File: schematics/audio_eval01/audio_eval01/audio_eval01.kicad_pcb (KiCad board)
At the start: 2 copper layers, 31.1 x 28.6 mm, 2 parts, among them J1 Conn_01x08_Pin

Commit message: Audio evaluation board work.
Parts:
- added C1: 0.1uF, Capacitor_SMD:C_0805_2012Metric_Pad1.18x1.45mm_HandSolder, F.Cu at (136.1, 83.0)
- added C10: 0.1uF, Capacitor_SMD:C_0805_2012Metric_Pad1.18x1.45mm_HandSolder, F.Cu at (150.5, 79.5)
- added C11: 22uF, Capacitor_SMD:C_0805_2012Metric_Pad1.18x1.45mm_HandSolder, F.Cu at (153.0, 79.5)
- added C12: 0.1uF, Capacitor_SMD:C_0805_2012Metric_Pad1.18x1.45mm_HandSolder, F.Cu at (144.8, 76.6)
- added C13: 10uF, Capacitor_SMD:C_0805_2012Metric_Pad1.18x1.45mm_HandSolder, F.Cu at (144.8, 74.0)
- added C2: 10uF, Capacitor_SMD:C_0805_2012Metric_Pad1.18x1.45mm_HandSolder, F.Cu at (138.6, 83.0)
- added C25: 47uF, Capacitor_Tantalum_SMD:CP_EIA-3216-18_Kemet-A, F.Cu at (152.0, 95.4)
- added C3: 10uF, Capacitor_SMD:C_0805_2012Metric_Pad1.18x1.45mm_HandSolder, F.Cu at (138.8, 99.2)
- added C4: 0.1uF, Capacitor_SMD:C_0805_2012Metric_Pad1.18x1.45mm_HandSolder, F.Cu at (137.0, 78.5)
- added C5: 10uF, Capacitor_SMD:C_0805_2012Metric_Pad1.18x1.45mm_HandSolder, F.Cu at (139.5, 78.5)
- added C6: 0.1uF, Capacitor_SMD:C_0805_2012Metric_Pad1.18x1.45mm_HandSolder, F.Cu at (150.5, 88.5)
- added C7: 10uF, Capacitor_SMD:C_0805_2012Metric_Pad1.18x1.45mm_HandSolder, F.Cu at (153.0, 88.5)
- added C8: 0.1uF, Capacitor_SMD:C_0805_2012Metric_Pad1.18x1.45mm_HandSolder, F.Cu at (153.0, 84.0)
- added C9: 22uF, Capacitor_SMD:C_0805_2012Metric_Pad1.18x1.45mm_HandSolder, F.Cu at (150.5, 84.0)
- added J2: AudioJack3, Connector_Audio:Jack_3.5mm_Switronic_ST-005-G_horizontal, F.Cu at (166.9, 94.2)
- added J3: Conn_01x02_Pin, Connector_PinHeader_2.54mm:PinHeader_1x02_P2.54mm_Vertical, F.Cu at (168.8, 78.5)
- added R1: R, Resistor_SMD:R_0805_2012Metric_Pad1.20x1.40mm_HandSolder, F.Cu at (142.0, 89.0)
- added R3: R, Resistor_SMD:R_0805_2012Metric_Pad1.20x1.40mm_HandSolder, F.Cu at (144.5, 89.0)
- added U2: AMS1117-1.8, Package_TO_SOT_SMD:SOT-223-3_TabPin2, F.Cu at (145.6, 96.7)
- J1: value Conn_01x08_Pin -> Conn_01x10_Pin; footprint Connector_PinHeader_2.54mm:PinHeader_1x08_P2.54mm_Vertical -> Connector_PinHeader_2.54mm:PinHeader_1x10_P2.54mm_Vertical
- moved U1 4.91 mm to (145.1, 83.0)
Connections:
- J1 pad 1: WCLK -> GND
- J1 pad 2: BCLK -> GPIO1
- J1 pad 3: MCLK -> DIN
- J1 pad 4: SDA -> WCLK
- J1 pad 5: SCL -> BCLK
- J1 pad 6: unconnected-(J1-Pin_6-Pad6) -> MCLK
- J1 pad 7: unconnected-(J1-Pin_7-Pad7) -> SDA
- J1 pad 8: GPIO1 -> SCL
- U1 pad 13: unconnected-(U1-AIN1-Pad13) -> GND
- U1 pad 14: unconnected-(U1-AIN2-Pad14) -> GND
- U1 pad 17: unconnected-(U1-AVDD-Pad17) -> 3V3
- U1 pad 19: unconnected-(U1-SPKM-Pad19) -> Net-(J3-Pin_1)
- U1 pad 2: unconnected-(U1-IOVDD-Pad2) -> 3V3
- U1 pad 21: unconnected-(U1-SPKVDD-Pad21) -> 5V0
- U1 pad 22: unconnected-(U1-SPKP-Pad22) -> Net-(J3-Pin_2)
- U1 pad 23: unconnected-(U1-SPKM-Pad23) -> Net-(J3-Pin_1)
- U1 pad 24: unconnected-(U1-SPKVDD-Pad24) -> 5V0
- U1 pad 26: unconnected-(U1-SPKP-Pad26) -> Net-(J3-Pin_2)
- U1 pad 27: unconnected-(U1-HPL-Pad27) -> Net-(U1-HPL)
- U1 pad 28: unconnected-(U1-HPVDD-Pad28) -> 3V3
- U1 pad 3: unconnected-(U1-DVDD-Pad3) -> 1V8
- U1 pad 30: unconnected-(U1-HPR-Pad30) -> Net-(U1-HPR)
- U1 pad 5: unconnected-(U1-DIN-Pad5) -> DIN
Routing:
- net 3V3: track 0.00 -> 93.9 mm
- net Net-(U1-HPL): track 0.00 -> 55.7 mm
- net 5V0: track 0.00 -> 46.8 mm, vias 0 -> 1
- net Net-(J3-Pin_2): track 0.00 -> 41.6 mm
- net Net-(U1-HPR): track 0.00 -> 32.0 mm, vias 0 -> 1
- net 1V8: track 0.00 -> 28.6 mm
- net SCL: track 0.00 -> 26.5 mm, vias 0 -> 1
- net Net-(J3-Pin_1): track 0.00 -> 22.7 mm
- net SDA: track 0.00 -> 17.0 mm, vias 0 -> 1
- net GPIO1: track 0.00 -> 15.8 mm, vias 0 -> 1
- net GND: track 0.00 -> 15.7 mm, vias 0 -> 17
- net DIN: track 0.00 -> 15.1 mm, vias 0 -> 1
- net MCLK: track 0.00 -> 14.8 mm, vias 0 -> 1
- net BCLK: track 0.00 -> 14.5 mm, vias 0 -> 1
- net WCLK: track 0.00 -> 14.4 mm, vias 0 -> 1
- added copper zone on B.Cu, net GND
- added copper zone on F.Cu, net GND
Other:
- board size 31.1 x 28.6 mm -> 47.3 x 33.6 mm
- board text added: "3V3"
- board text added: "5V0"
- board text added: "BCLK"
- board text added: "DIN"
- board text added: "GND"
- board text added: "GPIO1"
- board text added: "MCLK"
- board text added: "SCL"
- board text added: "SDA"
- board text added: "SPK+"
- board text added: "SPK-"
- board text added: "WCLK"

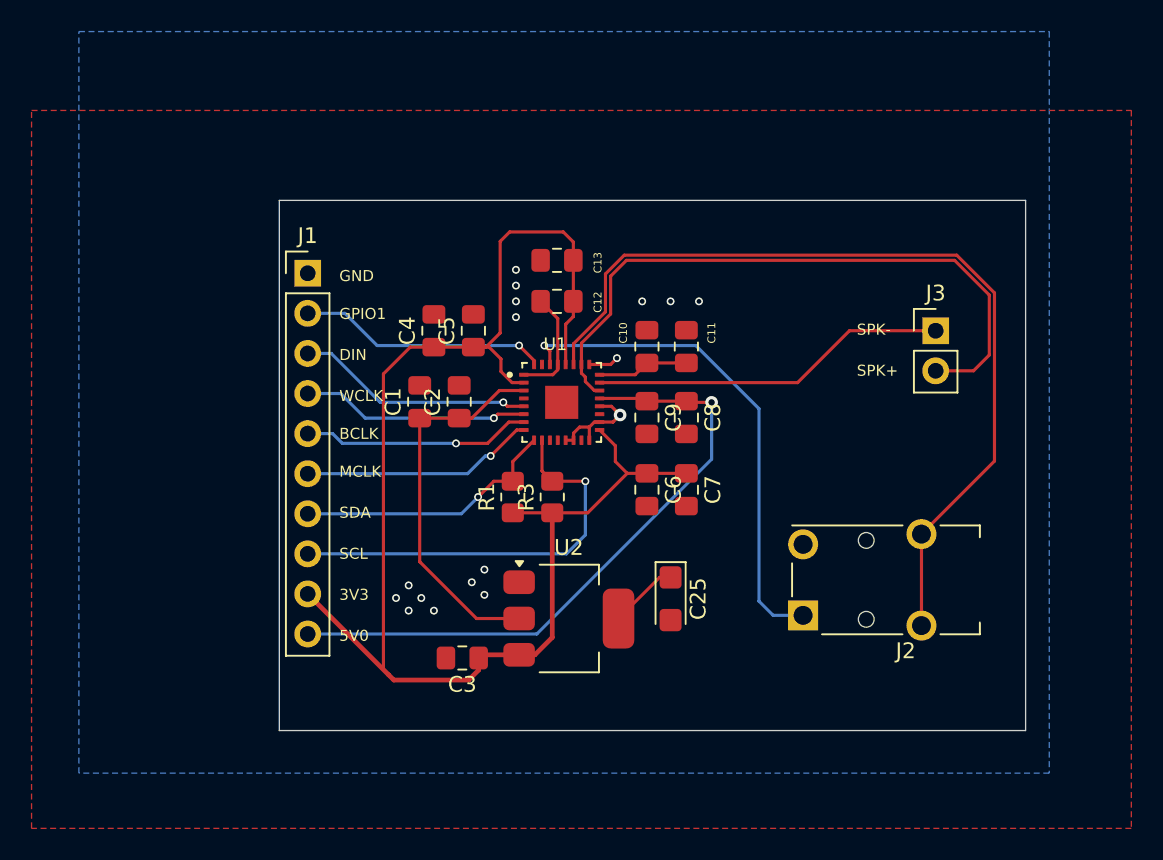
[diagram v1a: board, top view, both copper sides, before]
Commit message: Minor DRC fixes to Audio evaluation board.
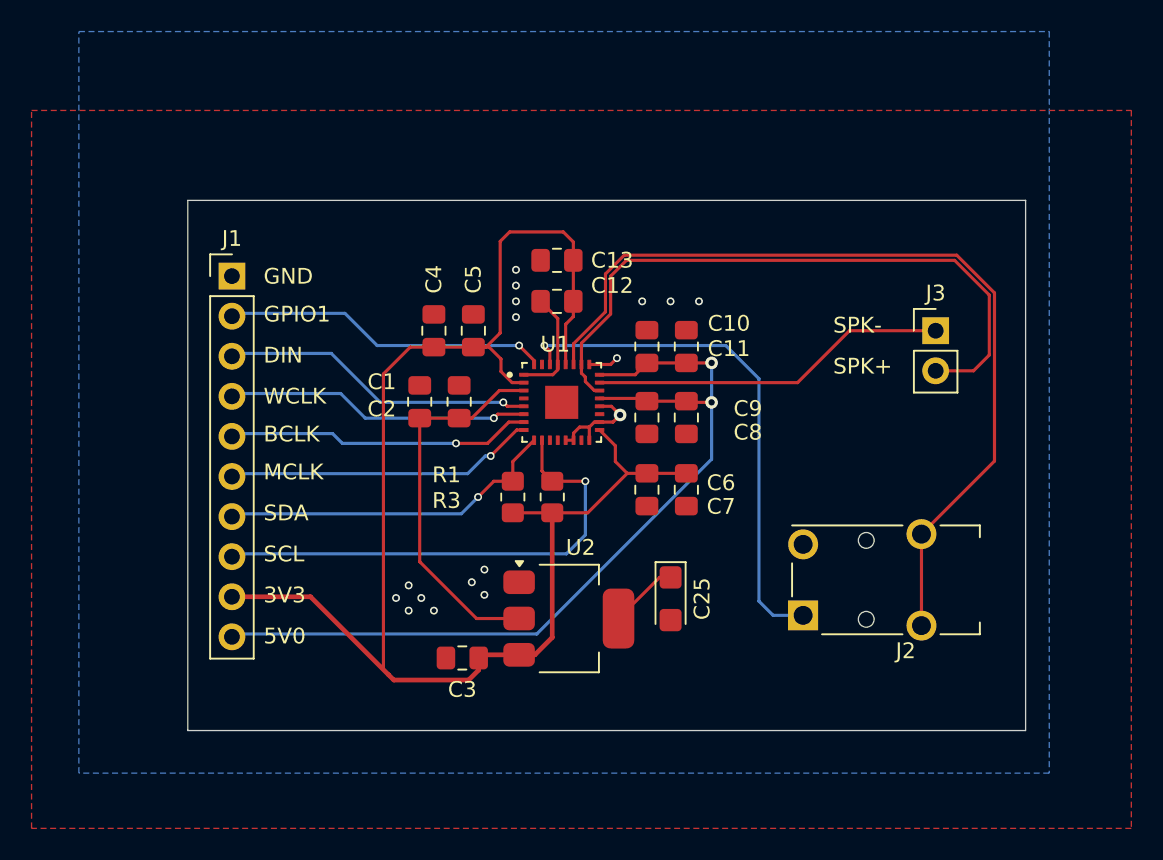
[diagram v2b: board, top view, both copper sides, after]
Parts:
- moved J1 4.80 mm to (124.2, 75.0)
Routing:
- net 5V0: track 46.8 -> 55.8 mm, vias 1 -> 2
- net MCLK: track 14.8 -> 19.7 mm
- net WCLK: track 14.4 -> 19.3 mm
- net SCL: track 26.5 -> 31.3 mm
- net GPIO1: track 15.8 -> 20.7 mm
- net SDA: track 17.0 -> 21.9 mm
- net DIN: track 15.1 -> 20.0 mm
- net BCLK: track 14.5 -> 19.4 mm
- net 3V3: track 93.9 -> 98.7 mm
- net Net-(U1-HPR): track 32.0 -> 33.1 mm
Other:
- board size 47.3 x 33.6 mm -> 53.1 x 33.6 mm

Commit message: Prepared Audio evaluation board for manufacture.
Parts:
- R1, R3: value R -> 4k7
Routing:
- net 1V8: track 28.6 -> 37.6 mm, vias 0 -> 2
- net Net-(J3-Pin_1): track 22.7 -> 27.4 mm, vias 0 -> 2
- net GND: track 15.7 -> 16.7 mm, vias 17 -> 19
- net 3V3: track 98.7 -> 97.9 mm

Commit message: Reset circuit added to audio evaluation board.
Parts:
- added C14: 0.1uF, Capacitor_SMD:C_0805_2012Metric_Pad1.18x1.45mm_HandSolder, F.Cu at (136.4, 72.3)
- added R2: 4k7, Resistor_SMD:R_0805_2012Metric_Pad1.20x1.40mm_HandSolder, F.Cu at (136.4, 74.7)
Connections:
- U1 pad 31: unconnected-(U1-~{RESET}-Pad31) -> ~{RESET}
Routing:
- net ~{RESET}: track 0.00 -> 12.3 mm, vias 0 -> 2
- net 3V3: track 97.9 -> 102.7 mm
- net GND: vias 19 -> 18

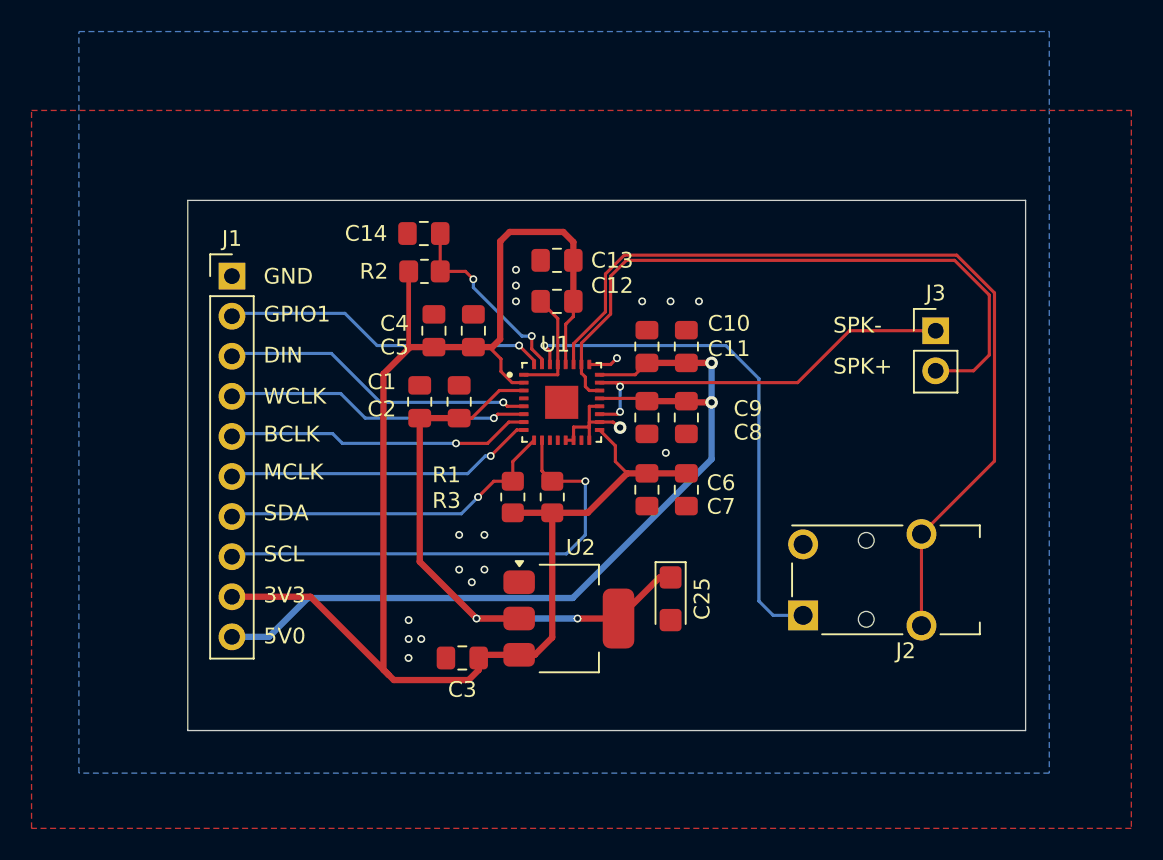
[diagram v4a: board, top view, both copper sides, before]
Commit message: Audio eval PCB sent to manufacturing.
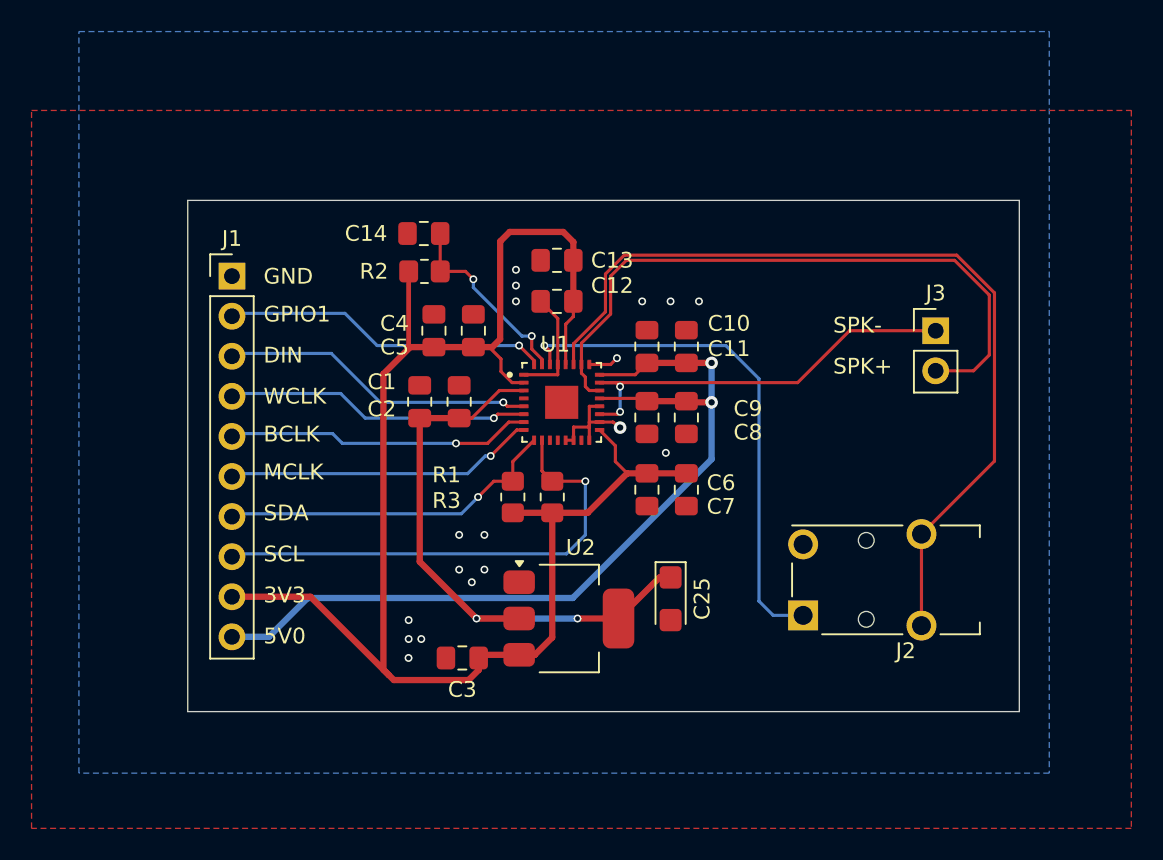
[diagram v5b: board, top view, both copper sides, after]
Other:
- board size 53.1 x 33.6 mm -> 52.7 x 32.4 mm
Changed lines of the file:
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@@
 	(gr_rect
 		(start 121.4 70.2)
-		(end 174.5 103.8)
+		(end 174.1 102.6)
 		(stroke
 			(width 0.05)
